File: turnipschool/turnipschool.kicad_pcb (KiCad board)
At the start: 4 copper layers, 22.5 x 12 mm, 62 parts, among them J1 USB-DEVICE-SHIELD, P1 CONN_1, P2 RESET_N, P3 DD, P4 DC, P5 3V3, P6 GND, P7 CABLE, T1 BALUN, U1 CC1111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

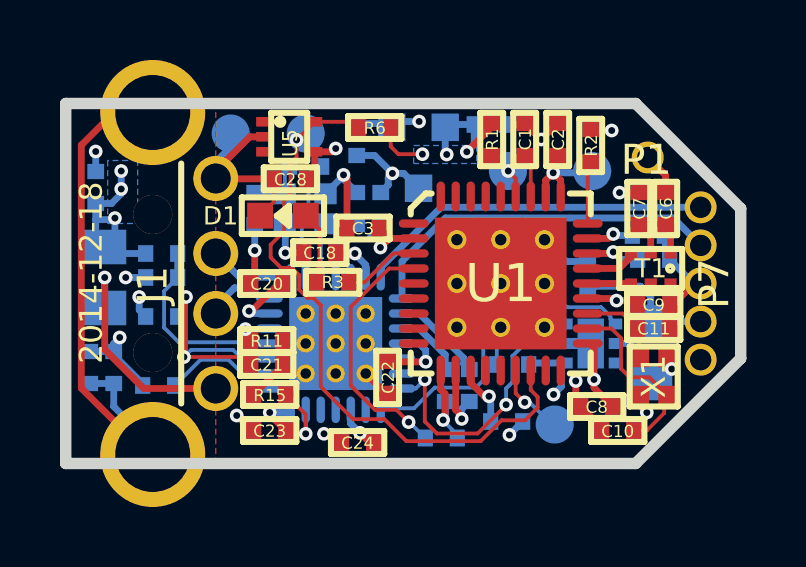
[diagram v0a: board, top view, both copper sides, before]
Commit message: updated date on silkscreen
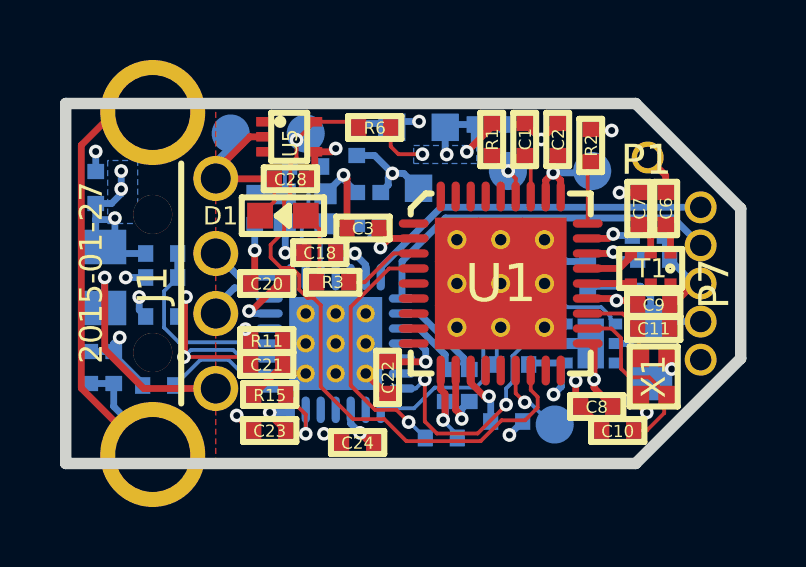
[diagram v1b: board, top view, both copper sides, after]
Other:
- board text added: "2015-01-27"
- board text removed: "2014-12-18"
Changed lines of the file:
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@@
     (pad_to_paste_clearance_ratio -0.05)
     (aux_axis_origin 0 0)
-    (visible_elements FFFF7FFF)
+    (visible_elements FFFFFF7F)
     (pcbplotparams
       (layerselection 0x010fc_80000007)
@@
     (effects (font (size 0.6096 0.6096) (thickness 0.127)) (justify mirror))
   )
-  (gr_text 2014-12-18 (at 90.85 89.64 90) (layer F.SilkS)
+  (gr_text 2015-01-27 (at 90.85 89.64 90) (layer F.SilkS)
     (effects (font (size 0.762 0.762) (thickness 0.1524)))
   )
